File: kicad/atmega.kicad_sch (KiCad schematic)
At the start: 30 parts, among them J1 Conn_01x04_Pin, J3 Conn_02x03_Odd_Even, J4 Conn_01x03_Pin, J5 Conn_01x06_Pin, J6 Conn_01x04_Pin, SW1 SW_Push, U1 ATmega164P-20P, Y1 18.432MHz

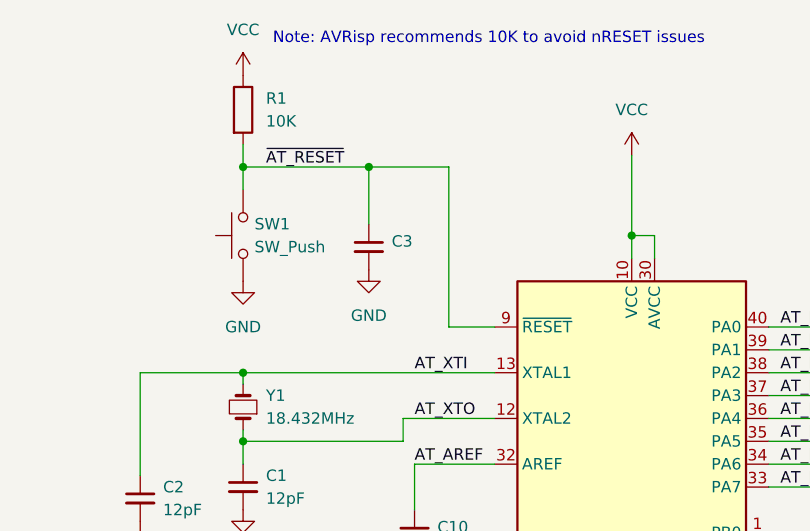
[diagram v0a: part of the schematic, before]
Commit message: pcb: move around stuff to make pcb smaller
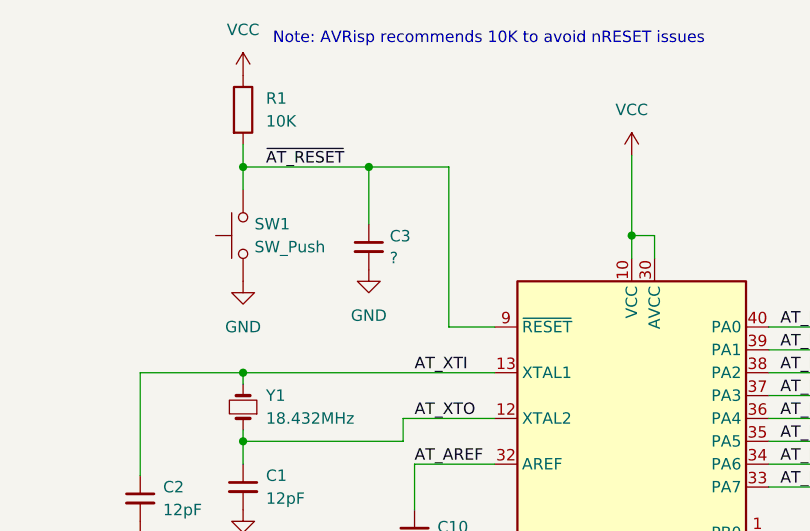
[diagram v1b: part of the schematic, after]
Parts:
- C3: value ~ -> ?; footprint Capacitor_THT:C_Disc_D4.3mm_W1.9mm_P5.00mm -> Capacitor_THT:C_Disc_D3.4mm_W2.1mm_P2.50mm
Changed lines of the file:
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@@
+	)
+	(symbol
+		(lib_id "Device:C_Small")
+		(at 91.44 40.64 0)
+		(unit 1)
+		(exclude_from_sim no)
+		(in_bom yes)
+		(on_board yes)
+		(dnp no)
+		(fields_autoplaced yes)
+		(property "Reference" "C3"
+			(at 93.7641 39.4341 0)
+			(effects
+				(font
+					(size 1.27 1.27)
+				)
+				(justify left)
+			)
+		)
+		(property "Value" "?"
+			(at 93.7641 41.8584 0)
+			(effects
+				(font
+					(size 1.27 1.27)
+				)
+				(justify left)
+			)
+		)
+		(property "Footprint" "Capacitor_THT:C_Disc_D3.4mm_W2.1mm_P2.50mm"
+			(at 91.44 40.64 0)
+			(effects
+				(font
+					(size 1.27 1.27)
+				)
+				(hide yes)
+			)
+		)
+		(property "Datasheet" "~"
+			(at 91.44 40.64 0)
+			(effects
+				(font
+					(size 1.27 1.27)
+				)
+				(hide yes)
+			)
+		)
+		(property "Description" "Unpolarized capacitor, small symbol"
+			(at 91.44 40.64 0)
+			(effects
+				(font
+					(size 1.27 1.27)
+				)
+				(hide yes)
+			)
+		)
+		(pin "2"
+		)
+		(pin "1"
+		)
+		(instances
+			(project "6502atty"
+				(path "/f612fa92-d5fa-4cb5-a666-c1c24e7cbb30/83b01514-6b56-4f3e-9a42-17260f217a5e"
+					(reference "C3")
+					(unit 1)
+				)
+			)
+		)
 	)
 	(symbol
@@
 					(unit 1)
 				)
-			)
-		)
-	)
-	(symbol
-		(lib_id "Device:C_Small")
-		(at 91.44 40.64 0)
-		(unit 1)
-		(exclude_from_sim no)
-		(in_bom yes)
-		(on_board yes)
-		(dnp no)
-		(fields_autoplaced yes)
-		(property "Reference" "C3"
-			(at 93.98 40.0112 0)
-			(effects
-				(font
-					(size 1.27 1.27)
-				)
-				(justify left)
-			)
-		)
-		(property "Value" "~"
-			(at 93.98 41.9163 0)
-			(effects
-				(font
-					(size 1.27 1.27)
-				)
-				(justify left)
-			)
-		)
-		(property "Footprint" "Capacitor_THT:C_Disc_D4.3mm_W1.9mm_P5.00mm"
-			(at 91.44 40.64 0)
-			(effects
-				(font
-					(size 1.27 1.27)
-				)
-				(hide yes)
-			)
-		)
-		(property "Datasheet" "~"
-			(at 91.44 40.64 0)
-			(effects
-				(font
-					(size 1.27 1.27)
-				)
-				(hide yes)
-			)
-		)
-		(property "Description" "Unpolarized capacitor, small symbol"
-			(at 91.44 40.64 0)
-			(effects
-				(font
-					(size 1.27 1.27)
-				)
-				(hide yes)
-			)
-		)
-		(pin "2"
-		)
-		(pin "1"
-		)
-		(instances
-			(project "6502atty"
-				(path "/f612fa92-d5fa-4cb5-a666-c1c24e7cbb30/83b01514-6b56-4f3e-9a42-17260f217a5e"
-					(reference "C3")
-					(unit 1)
-				)

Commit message: update to kicad10, v1_r3 release
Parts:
- C10: value ~ -> (none)
- R5: footprint Resistor_THT:R_Axial_DIN0207_L6.3mm_D2.5mm_P10.16mm_Horizontal -> Resistor_THT:R_Axial_DIN0207_L6.3mm_D2.5mm_P2.54mm_Vertical; KiLib_Generator (none) -> resistor/THT
